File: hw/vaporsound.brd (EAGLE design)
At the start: 100 x 80 mm, 57 parts

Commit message: schematics done-ish
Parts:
- removed IC1: (no value), SparkFun-PowerIC:SOT223
- added Q1, Q2: BSS138, SparkFun-DiscreteSemi:SOT23-3
- added R11, R12, R13, R14: 4k7, rcl:R0603
- added SV1: (no value), con-lstb:MA04-1
- added SV2: (no value), con-lstb:MA03-1
- added U$4: MA23-2, con-lstb-mod:MA23-2
- moved R7 84.8 mm to (6.69, 70.3), turned to 90 degrees
- moved C19 81.0 mm to (9.23, 69.0), turned to 90 degrees
- moved C18 77.2 mm to (11.8, 67.7), turned to 90 degrees
- moved C26 76.1 mm to (7.96, 62.6), turned to 270 degrees
- moved C29 74.8 mm to (85.4, 64.9), turned to 0 degrees
- moved C31 72.7 mm to (85.1, 53.3), turned to 180 degrees
- moved C32 71.8 mm to (85.1, 55.9), turned to 180 degrees
- moved L5 70.7 mm to (20.7, 69.0), turned to 270 degrees
- moved R8 70.1 mm to (6.69, 53.8), turned to 270 degrees
- moved C21 68.1 mm to (9.23, 55.0), turned to 270 degrees
- moved C20 66.2 mm to (11.8, 56.3), turned to 270 degrees
- moved R9 65.1 mm to (6.69, 46.1), turned to 90 degrees
- moved C28 61.4 mm to (77.0, 71.1), turned to 270 degrees
- moved C23 61.1 mm to (9.23, 44.9), turned to 90 degrees
- moved R10 59.6 mm to (6.69, 28.4), turned to 270 degrees
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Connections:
- new net N$24: C7.-, SV2.3
- new net N$29: C8.-, SV2.1
- new net SCL5V: Q2.3, R13.1, SV1.4
- new net SDA5V: Q1.3, R14.1, SV1.3
- net +3V3: now also Q1.1, Q2.1, R11.2, R12.2, U$4.3, U$4.4; no longer IC1.2, IC1.4
- net +5V: now also R13.2, R14.2, SV1.2, U$4.5, U$4.6; no longer IC1.3
- net BCK: now also U$4.31
- net D_ADC: now also U$4.30
- net D_AMP: now also U$4.28
- net GND: now also SV1.1, SV2.2, U$4.1, U$4.2, U$4.43, U$4.44, U$4.45, U$4.46; no longer IC1.1
- net LRCK: now also U$4.29
- net MCK: now also U$4.25
- net POWERDOWN: now also U$4.23
- net RESET: now also U$4.15
- net SCL: now also Q2.2, R12.1, U$4.19
- net SDA: now also Q1.2, R11.1, U$4.20
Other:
- outline, holes or cut-outs redrawn

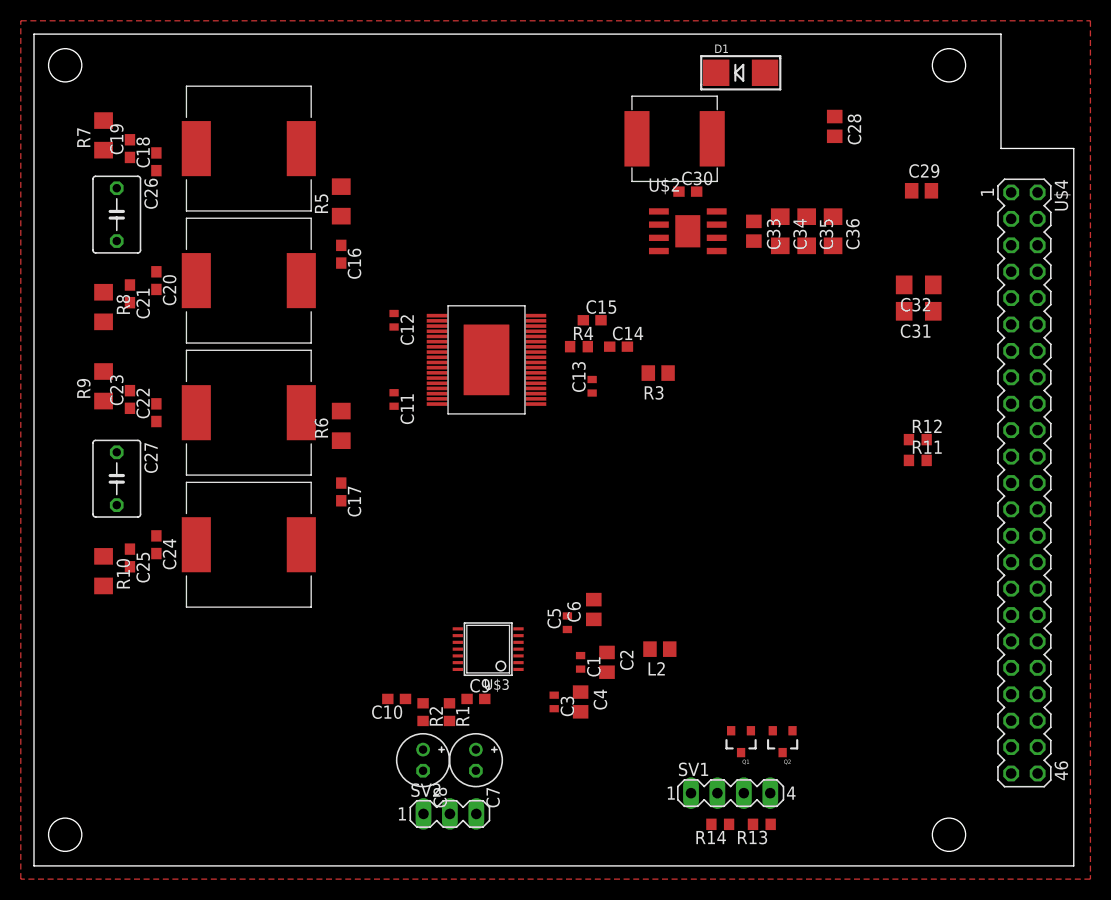
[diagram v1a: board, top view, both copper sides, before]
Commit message: layout voltage regulator and add some capacitors
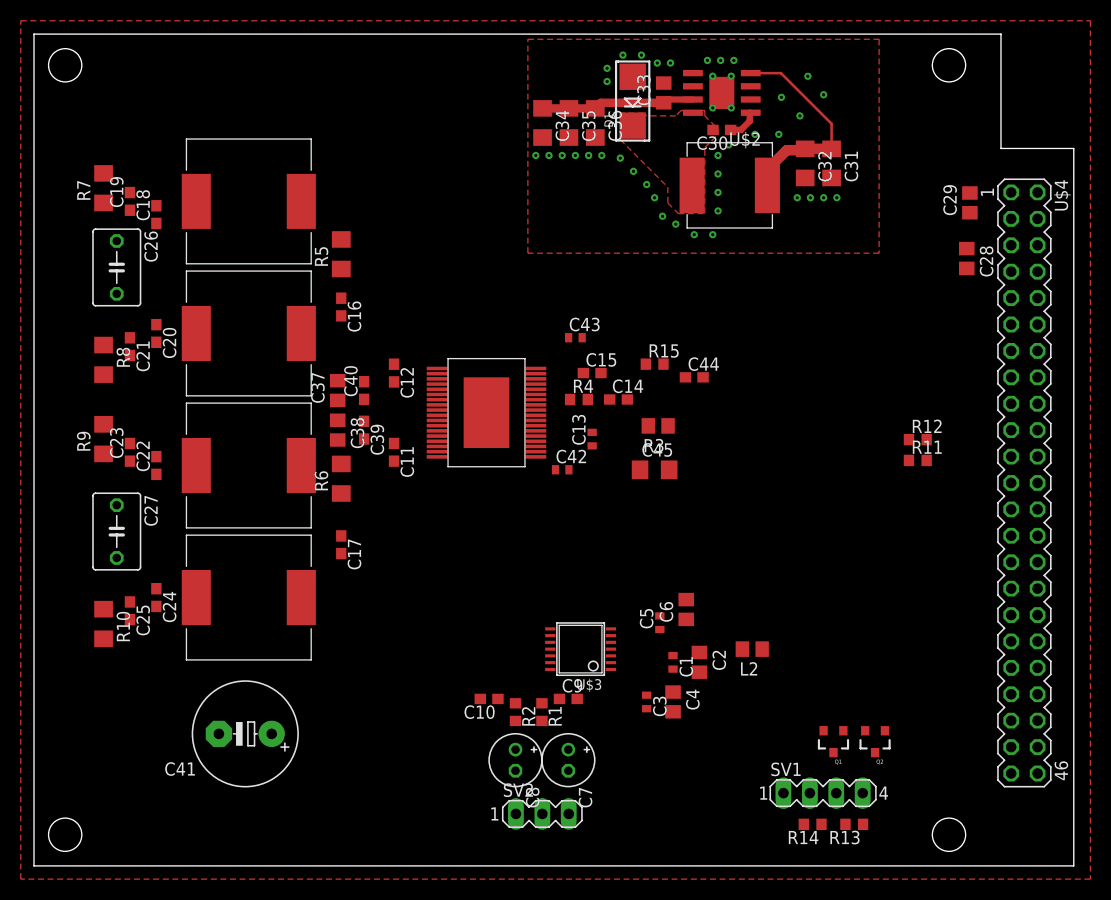
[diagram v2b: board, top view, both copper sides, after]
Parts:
- added C37, C38: 1u, rcl:C0805
- added C39, C40: 100n, rcl:C0603
- added C41: 1000u, rcl:E5-10,5
- added C42, C43: 100n, rcl:C0402
- added C44: 1n, rcl:C0603
- added C45: 22u, rcl:C1206
- added R15: 10k, rcl:R0603
- C11, C12: device rcl:C0402 -> rcl:C0603
- moved C34 25.1 mm to (48.9, 71.5)
- moved C35 25.1 mm to (51.5, 71.5)
- moved C36 25.1 mm to (54.0, 71.5)
- moved C28 18.0 mm to (89.7, 58.4)
- moved C31 16.5 mm to (76.7, 67.6), turned to 270 degrees
- moved C32 16.0 mm to (74.2, 67.6), turned to 270 degrees
- moved C33 15.9 mm to (60.6, 74.3), turned to 90 degrees
- moved U$2 13.7 mm to (66.2, 74.3), turned to 180 degrees
- moved D1 10.7 mm to (57.6, 73.5), turned to 90 degrees
- moved C1 8.89 mm to (61.5, 19.6)
- moved C10 8.89 mm to (43.8, 16.1)
- moved C2 8.89 mm to (64.0, 19.6)
- moved C3 8.89 mm to (58.9, 15.8)
- moved C4 8.89 mm to (61.5, 15.8)
- moved C5 8.89 mm to (60.2, 23.4)
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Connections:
- net N$23 renamed SW
- net +24V: now also C37.1, C38.1, C39.1, C40.1, C41.+
- net +3V3: now also C42.1, C43.1, C45.1, R15.2
- net GND: now also C37.2, C38.2, C39.2, C40.2, C41.-, C42.2, C43.2, C44.2, C45.2
- net RESET: now also C44.1, R15.1
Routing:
- net +5V: track 0.00 -> 20.7 mm
- net +24V: track 0.00 -> 14.8 mm
- net N$22: track 0.00 -> 3.09 mm
- added copper zone on layer 1, net SW

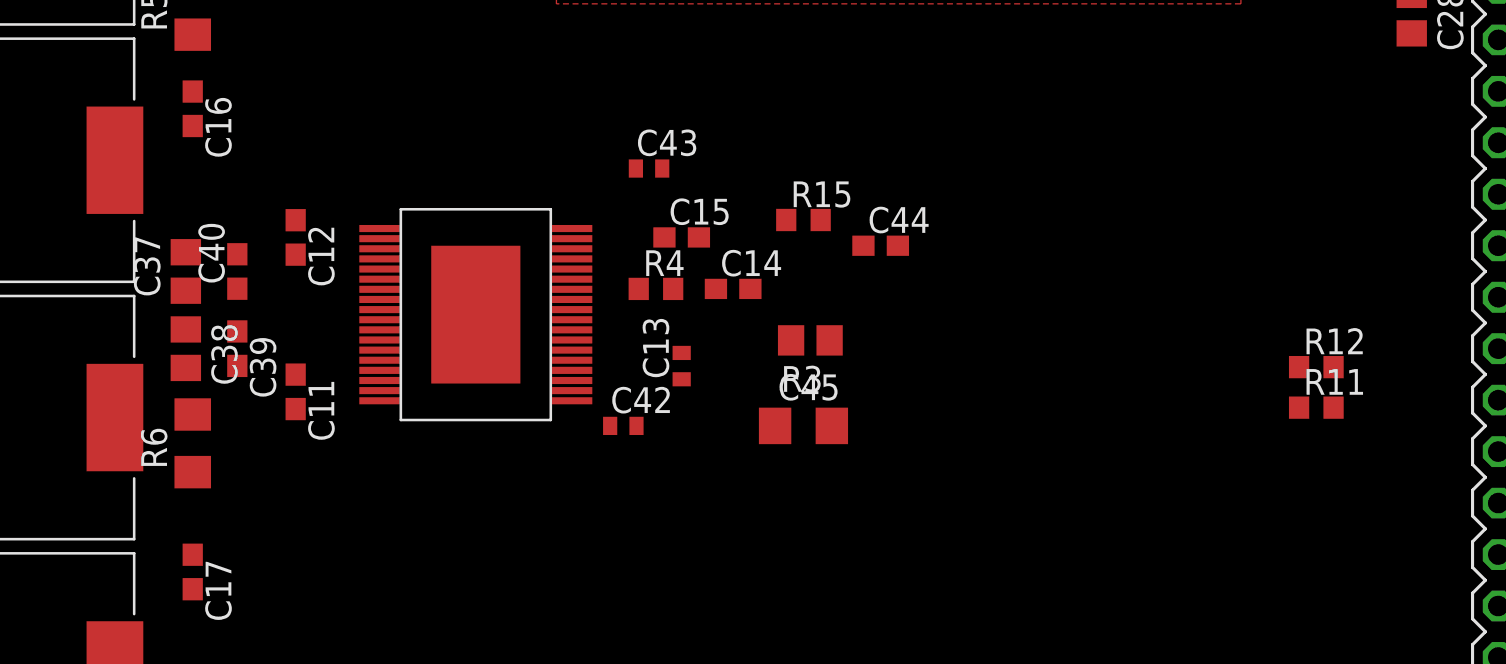
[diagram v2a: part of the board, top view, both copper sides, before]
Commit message: begin layout of 24v side of sta350
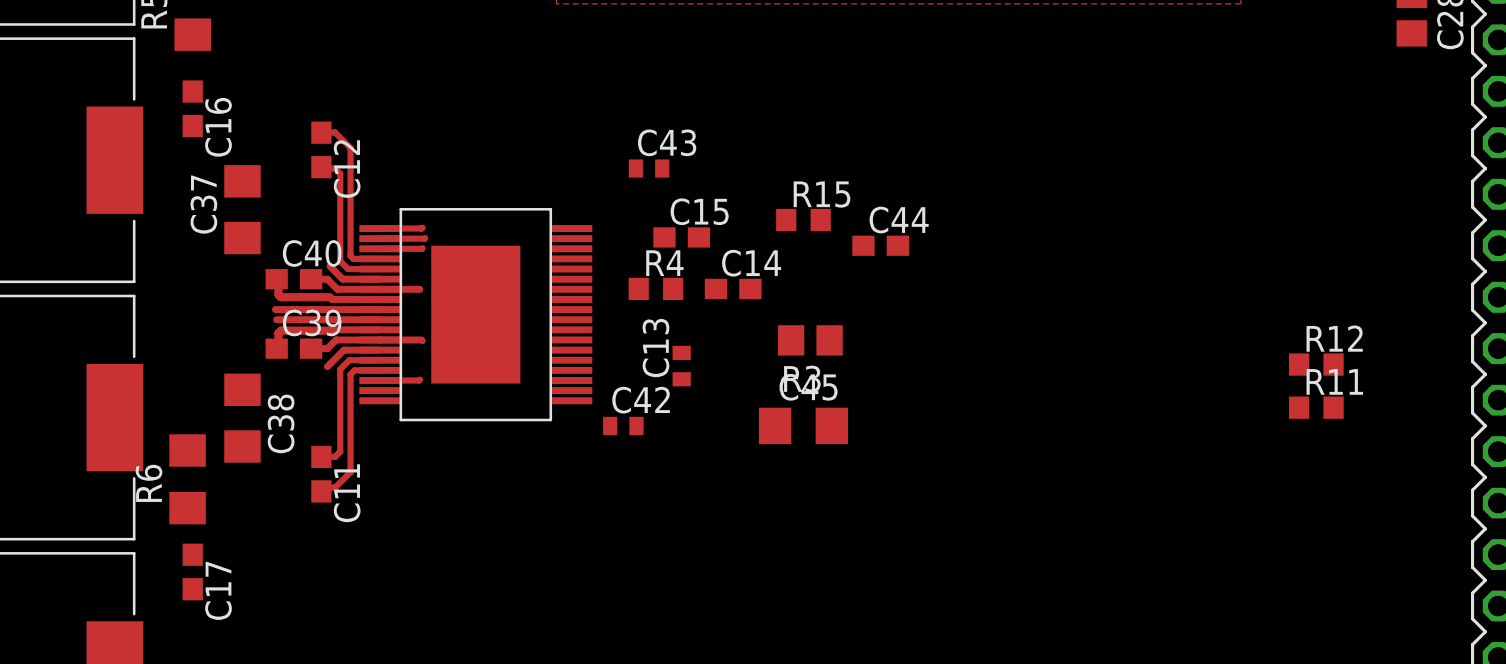
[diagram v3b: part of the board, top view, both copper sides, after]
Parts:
- C37, C38: device rcl:C0805 -> rcl:C1206
- moved C12 4.50 mm to (35.9, 51.7)
- moved C38 4.42 mm to (32.0, 38.5)
- moved C11 4.26 mm to (35.9, 35.7)
- moved C37 4.13 mm to (32.0, 48.8)
- moved C40 2.82 mm to (34.5, 45.3), turned to 0 degrees
- moved C39 2.79 mm to (34.5, 41.9), turned to 0 degrees
- moved R6 1.80 mm to (29.3, 35.5)
- moved R12 0.13 mm to (85.0, 41.1)
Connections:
- net N$14 renamed OUT2A
- net N$15 renamed OUT2B
- net N$16 renamed OUT1B
- net N$17 renamed OUT1A
- net N$18 renamed SPKR2B
- net N$20 renamed SPKR2A
- net N$25 renamed SPKR1B
- net N$26 renamed SPKR1A
- net N$6 renamed GND_REG
- net N$7 renamed VDD
- net N$8 renamed VSS
- net N$9 renamed VCC_REG
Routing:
- net GND: track 0.00 -> 19.8 mm
- net +24V: track 14.8 -> 26.6 mm
- net VSS: track 0.00 -> 8.58 mm
- net VDD: track 0.00 -> 8.17 mm
- net VCC_REG: track 0.00 -> 7.48 mm
- net GND_REG: track 0.00 -> 7.23 mm
- net OUT2A: track 0.00 -> 5.14 mm
- net OUT1B: track 0.00 -> 5.08 mm
- net OUT1A: track 0.00 -> 2.91 mm
- net OUT2B: track 0.00 -> 2.71 mm

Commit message: output stage almost routed
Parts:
- moved C41 31.0 mm to (17.7, 43.6)
- moved R9 21.4 mm to (9.88, 19.9), turned to 180 degrees
- moved R8 19.2 mm to (9.94, 67.6), turned to 180 degrees
- moved R10 19.0 mm to (25.4, 19.9), turned to 0 degrees
- moved R7 18.9 mm to (25.4, 67.6), turned to 0 degrees
- moved C23 17.9 mm to (8.86, 21.9), turned to 180 degrees
- moved C25 17.4 mm to (26.4, 21.9), turned to 0 degrees
- moved C19 17.3 mm to (26.4, 65.4), turned to 0 degrees
- moved C22 16.6 mm to (11.9, 21.9), turned to 180 degrees
- moved C21 15.5 mm to (8.92, 65.4), turned to 180 degrees
- moved C27 14.8 mm to (17.6, 20.9), turned to 0 degrees
- moved C20 14.2 mm to (12.0, 65.4), turned to 180 degrees
- moved C26 13.1 mm to (17.7, 66.3), turned to 180 degrees
- moved L3 12.7 mm to (11.0, 30.2), turned to 0 degrees
- moved C24 12.2 mm to (23.3, 21.9), turned to 0 degrees
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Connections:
- removed net N$13: C17.1, R6.1
- new net N$6: C17.2, R6.2
- net OUT1A: now also R6.1; no longer C17.2
- net OUT1B: now also C17.1; no longer R6.2
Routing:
- net N$6: track 0.00 -> 2.29 mm
- net N$12: track 0.00 -> 2.29 mm
- net VSS: track 8.58 -> 7.31 mm
- net VCC_REG: track 7.48 -> 6.21 mm
- net VDD: track 8.17 -> 7.28 mm
- net GND_REG: track 7.23 -> 6.34 mm
- net +24V: track 26.6 -> 25.8 mm, vias 0 -> 8
- net OUT2A: track 5.14 -> 4.63 mm
- net OUT1B: track 5.08 -> 4.57 mm
- net GND: vias 42 -> 56
- added copper zone on layer 1, net +24V
- added copper zone on layer 16, net +24V
- added copper zone on layer 16, net GND
- added copper zone on layer 1, net OUT1A
- added copper zone on layer 1, net OUT1B
- added copper zone on layer 1, net OUT2A
- added copper zone on layer 1, net OUT2B

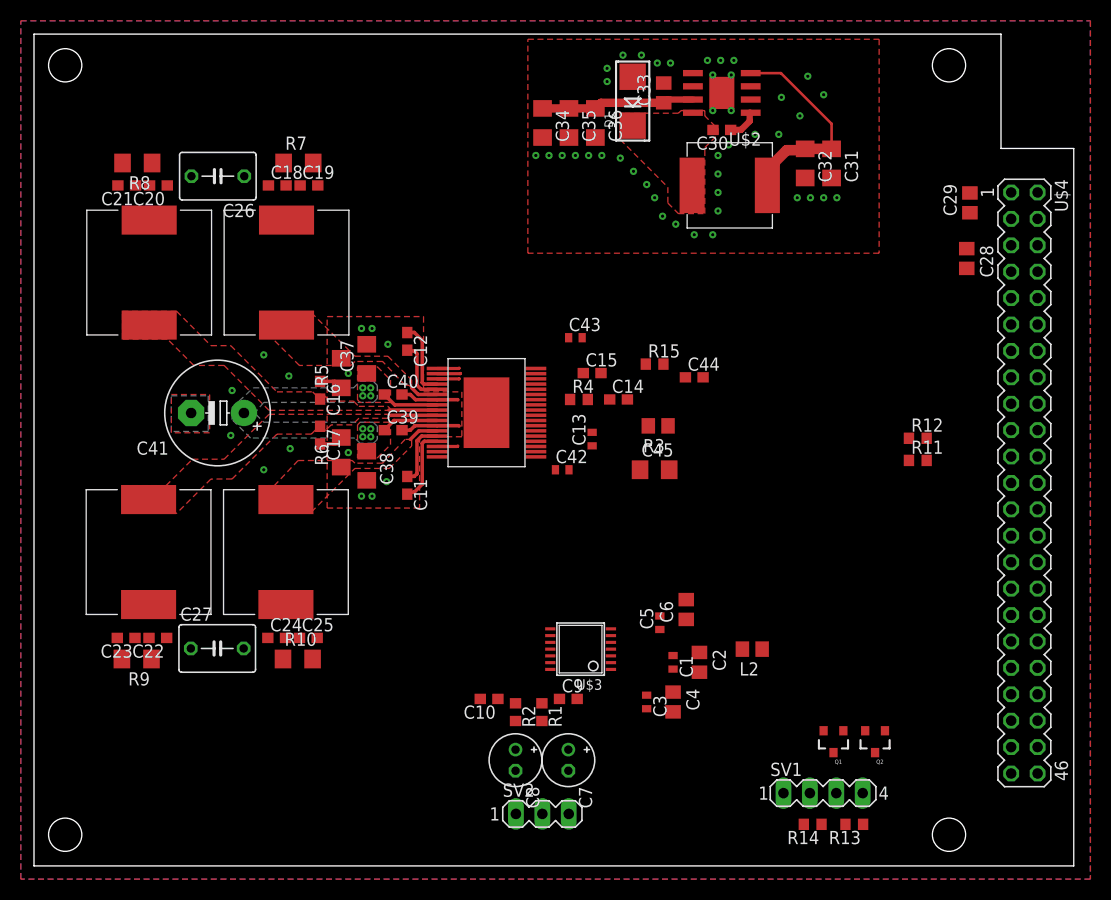
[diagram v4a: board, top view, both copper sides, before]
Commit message: begin component placement at input side of sta350
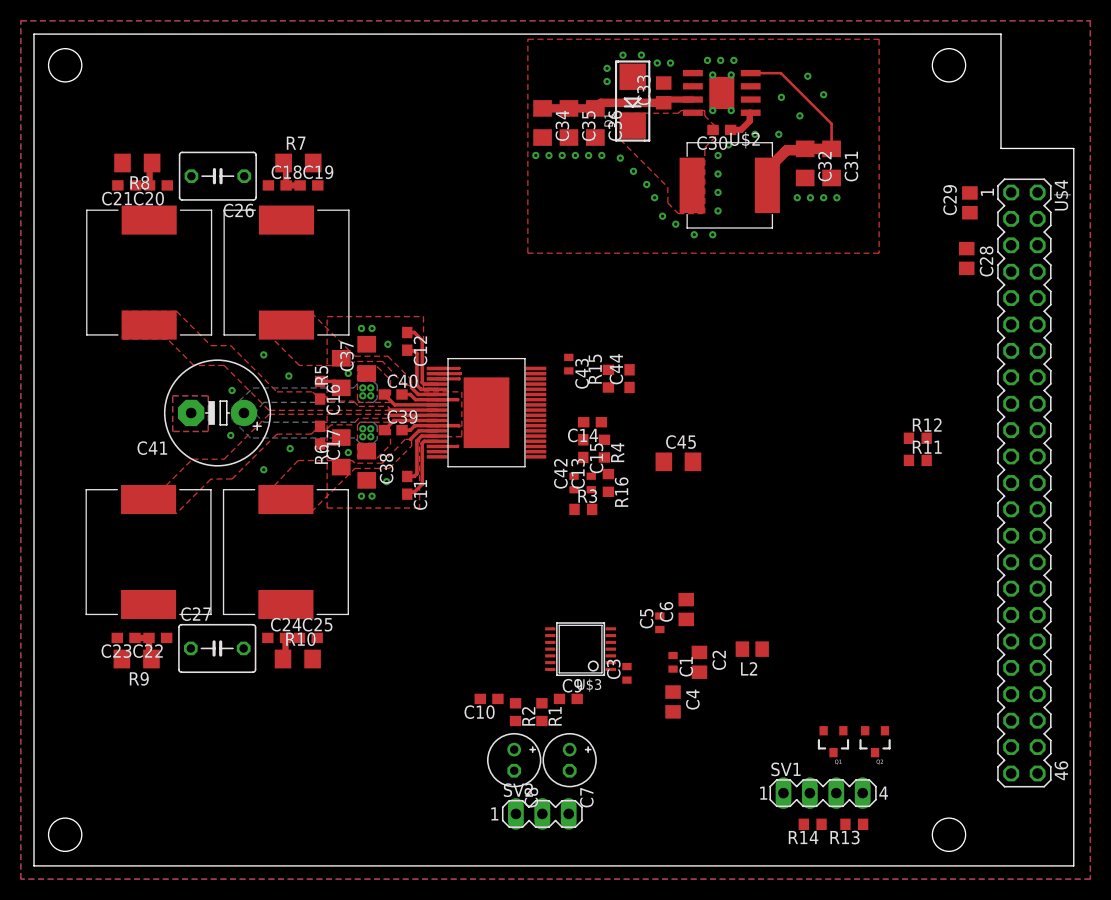
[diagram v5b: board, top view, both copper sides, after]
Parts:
- added R16: 0r, rcl:R0603
- R3: device rcl:R0805 -> rcl:R0603
- moved R3 10.8 mm to (52.8, 34.3), turned to 0 degrees
- moved C15 7.32 mm to (52.8, 40.1), turned to 270 degrees
- moved C44 6.22 mm to (57.3, 46.9), turned to 90 degrees
- moved R4 5.33 mm to (54.9, 40.1), turned to 270 degrees
- moved R15 4.66 mm to (55.2, 46.9), turned to 90 degrees
- moved C13 4.22 mm to (53.6, 36.8)
- moved C3 3.34 mm to (57.0, 18.5), turned to 90 degrees
- moved C14 3.32 mm to (53.7, 42.7), turned to 180 degrees
- moved C43 2.62 mm to (51.4, 48.3), turned to 270 degrees
- moved C45 2.41 mm to (62.0, 38.9)
- moved C42 1.71 mm to (51.9, 36.8), turned to 90 degrees
- moved C7 0.13 mm to (51.5, 10.2)
- moved C8 0.13 mm to (46.2, 10.2)
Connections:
- net N$1 renamed ADC_VREF
- net N$10 renamed FILTER_PLL
- net N$2 renamed C_RIGHT
- net N$22 renamed BOOST
- net N$24 renamed RIGHT_INPUT
- net N$29 renamed LEFT_INPUT
- net N$3 renamed VIN_R
- net N$4 renamed VIN_L
- net N$5 renamed C_LEFT
- new net AGND: C13.2, C14.2, C15.2, R16.1, U$1.P$26
- net GND: now also R16.2; no longer C13.2, C14.2, C15.2, U$1.P$26
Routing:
- net N$21: track 0.00 -> 3.61 mm
- net N$19: track 0.00 -> 3.61 mm
- net N$28: track 0.00 -> 3.48 mm
- net N$27: track 0.00 -> 3.48 mm
